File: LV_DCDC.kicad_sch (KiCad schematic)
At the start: 8 parts, among them J1 1017503, J2 1017503

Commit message: made todo, added power
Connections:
- net at R4.2, R5.1, R6.1: no longer C9.1
- net at R6.2: now also C9.1
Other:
- added sheet power (power.kicad_sch)
- sheet CAN ports: added CANH, CANL, RXD, TXD; removed none
- sheet uC ports: added CANRx, CANTx; removed none
- note added: "TODO: BIG DCDC connhector thermistors big decouple V sense and feedback current sense"
- moved on the sheet: C9, R6
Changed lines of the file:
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@@
 	(generator_version "9.0")
 	(paper "A3")
+	(text "TODO:\nBIG DCDC connhector\nthermistors\nbig decouple\nV sense and feedback\ncurrent sense"
+		(exclude_from_sim no)
+		(at 316.738 168.91 0)
+		(effects
+			(font
+				(size 5.08 5.08)
+			)
+		)
+	)
 	(text "BCM4414xG0F4440yzz"
 		(exclude_from_sim no)
@@
 	)
 	(junction
-		(at 295.91 92.71)
-		(diameter 0)
-		(color 0 0 0 0)
-	)
-	(junction
 		(at 240.03 67.31)
 		(diameter 0)
@@
 	)
 	(junction
+		(at 334.01 74.93)
+		(diameter 0)
+		(color 0 0 0 0)
+	)
+	(junction
+		(at 54.61 67.31)
+		(diameter 0)
+		(color 0 0 0 0)
+	)
+	(junction
 		(at 281.94 92.71)
 		(diameter 0)
@@
 	)
 	(junction
-		(at 334.01 74.93)
-		(diameter 0)
-		(color 0 0 0 0)
-	)
-	(junction
-		(at 54.61 67.31)
-		(diameter 0)
-		(color 0 0 0 0)
-	)
-	(junction
 		(at 349.25 67.31)
 		(diameter 0)
@@
 	(wire
 		(pts
+			(xy 281.94 92.71) (xy 293.37 92.71)
+		)
+		(stroke
+			(width 0)
+			(type default)
+		)
+	)
+	(wire
+		(pts
 			(xy 54.61 72.39) (xy 60.96 72.39)
 		)
@@
 	(wire
 		(pts
-			(xy 281.94 96.52) (xy 281.94 92.71)
-		)
-		(stroke
-			(width 0)
-			(type default)
-		)
-	)
-	(wire
-		(pts
-			(xy 295.91 92.71) (xy 295.91 96.52)
-		)
-		(stroke
-			(width 0)
-			(type default)
-		)
-	)
-	(wire
-		(pts
 			(xy 166.37 125.73) (xy 247.65 125.73)
 		)
@@
 	(wire
 		(pts
+			(xy 300.99 92.71) (xy 304.8 92.71)
+		)
+		(stroke
+			(width 0)
+			(type default)
+		)
+	)
+	(wire
+		(pts
 			(xy 43.18 72.39) (xy 54.61 72.39)
 		)
@@
 	(wire
 		(pts
+			(xy 281.94 92.71) (xy 281.94 96.52)
+		)
+		(stroke
+			(width 0)
+			(type default)
+		)
+	)
+	(wire
+		(pts
 			(xy 166.37 67.31) (xy 240.03 67.31)
 		)
@@
 	(wire
 		(pts
-			(xy 295.91 92.71) (xy 303.53 92.71)
+			(xy 360.68 99.06) (xy 368.3 99.06)
 		)
 		(stroke
@@
 	(wire
 		(pts
+			(xy 304.8 92.71) (xy 304.8 96.52)
+		)
+		(stroke
+			(width 0)
+			(type default)
+		)
+	)
+	(wire
+		(pts
 			(xy 29.21 72.39) (xy 43.18 72.39)
 		)
@@
 	(wire
 		(pts
-			(xy 281.94 92.71) (xy 295.91 92.71)
-		)
-		(stroke
-			(width 0)
-			(type default)
-		)
-	)
-	(wire
-		(pts
 			(xy 334.01 64.77) (xy 334.01 67.31)
 		)
@@
 		(pts
 			(xy 344.17 74.93) (xy 349.25 74.93)
+		)
+		(stroke
+			(width 0)
+			(type default)
+		)
+	)
+	(wire
+		(pts
+			(xy 360.68 96.52) (xy 368.3 96.52)
 		)
 		(stroke
@@
 	(symbol
 		(lib_id "Device:C")
-		(at 295.91 100.33 0)
+		(at 304.8 100.33 0)
 		(unit 1)
 		(exclude_from_sim no)
@@
 		(fields_autoplaced yes)
 		(property "Reference" "C9"
-			(at 299.72 99.0599 0)
+			(at 308.61 99.0599 0)
 			(effects
 				(font
@@
 		)
 		(property "Value" "100nF"
-			(at 299.72 101.5999 0)
+			(at 308.61 101.5999 0)
 			(effects
 				(font
@@
 		)
 		(property "Footprint" ""
-			(at 296.8752 104.14 0)
+			(at 305.7652 104.14 0)
 			(effects
 				(font
@@
 		)
 		(property "Datasheet" "~"
-			(at 295.91 100.33 0)
+			(at 304.8 100.33 0)
 			(effects
 				(font
@@
 		)
 		(property "Description" "Unpolarized capacitor"
-			(at 295.91 100.33 0)
+			(at 304.8 100.33 0)
 			(effects
 				(font
@@
 	(symbol
 		(lib_id "power:GND")
-		(at 295.91 104.14 0)
+		(at 304.8 104.14 0)
 		(unit 1)
 		(exclude_from_sim no)
@@
 		(fields_autoplaced yes)
 		(property "Reference" "#PWR026"
-			(at 295.91 110.49 0)
+			(at 304.8 110.49 0)
 			(effects
 				(font
@@
 		)
 		(property "Value" "GND"
-			(at 295.91 109.22 0)
+			(at 304.8 109.22 0)
 			(effects
 				(font
@@
 		)
 		(property "Footprint" ""
-			(at 295.91 104.14 0)
+			(at 304.8 104.14 0)
 			(effects
 				(font
@@
 		)
 		(property "Datasheet" ""
-			(at 295.91 104.14 0)
+			(at 304.8 104.14 0)
 			(effects
 				(font
@@
 		)
 		(property "Description" "Power symbol creates a global label with name \"GND\" , ground"
-			(at 295.91 104.14 0)
+			(at 304.8 104.14 0)
 			(effects
 				(font
@@
 	(symbol
 		(lib_id "Device:R")
-		(at 307.34 92.71 90)
+		(at 297.18 92.71 90)
 		(unit 1)
 		(exclude_from_sim no)
@@
 		(fields_autoplaced yes)
 		(property "Reference" "R6"
-			(at 307.34 86.36 90)
+			(at 297.18 86.36 90)
 			(effects
 				(font
@@
 		)
 		(property "Value" "1k"
-			(at 307.34 88.9 90)
+			(at 297.18 88.9 90)
 			(effects
 				(font
@@
 		)
 		(property "Footprint" ""
-			(at 307.34 94.488 90)
+			(at 297.18 94.488 90)
 			(effects
 				(font
@@
 		)
 		(property "Datasheet" "~"
-			(at 307.34 92.71 0)
+			(at 297.18 92.71 0)
 			(effects
 				(font
@@
 		)
 		(property "Description" "Resistor"
-			(at 307.34 92.71 0)
+			(at 297.18 92.71 0)
 			(effects
 				(font
@@
 	)
 	(sheet
-		(at 337.82 157.48)
-		(size 25.4 16.51)
+		(at 204.47 176.53)
+		(size 13.97 17.78)
 		(exclude_from_sim no)
 		(in_bom yes)
@@
 			(color 0 0 0 0.0000)
 		)
+		(property "Sheetname" "power"
+			(at 204.47 175.8184 0)
+			(effects
+				(font
+					(size 1.27 1.27)
+				)
+				(justify left bottom)
+			)
+		)
+		(property "Sheetfile" "power.kicad_sch"
+			(at 204.47 194.8946 0)
+			(effects
+				(font
+					(size 1.27 1.27)
+				)
+				(justify left top)
+			)
+		)
+		(instances
+			(project "LV_DCDC"
+				(path "/ccad4640-78c7-423b-83df-3ec0b90aa2b3"
+					(page "4")
+				)
+			)
+		)
+	)
+	(sheet
+		(at 368.3 92.71)
+		(size 16.51 10.16)
+		(exclude_from_sim no)
+		(in_bom yes)
+		(on_board yes)
+		(dnp no)
+		(fields_autoplaced yes)
+		(stroke
+			(width 0.1524)
+			(type solid)
+		)
+		(fill
+			(color 0 0 0 0.0000)
+		)
 		(property "Sheetname" "CAN"
-			(at 337.82 156.7684 0)
+			(at 368.3 91.9984 0)
 			(effects
 				(font
@@
 		)
 		(property "Sheetfile" "CAN.kicad_sch"
-			(at 337.82 174.5746 0)
+			(at 368.3 103.4546 0)
 			(effects
 				(font
@@
 				)
 				(justify left top)
+			)
+		)
+		(pin "TXD" input
+			(at 368.3 96.52 180)
+			(effects
+				(font
+					(size 1.27 1.27)
+				)
+				(justify left)
+			)
+		)
+		(pin "CANL" input
+			(at 384.81 99.06 0)
+			(effects
+				(font
+					(size 1.27 1.27)
+				)
+				(justify right)
+			)
+		)
+		(pin "RXD" output
+			(at 368.3 99.06 180)
+			(effects
+				(font
+					(size 1.27 1.27)
+				)
+				(justify left)
+			)
+		)
+		(pin "CANH" input
+			(at 384.81 96.52 0)
+			(effects
+				(font
+					(size 1.27 1.27)
+				)
+				(justify right)
 			)
 		)
@@
 	)
 	(sheet
-		(at 273.05 146.05)
+		(at 337.82 92.71)
 		(size 22.86 20.32)
 		(exclude_from_sim no)
@@
 		)
 		(property "Sheetname" "uC"
-			(at 273.05 145.3384 0)
+			(at 337.82 91.9984 0)
 			(effects
 				(font
@@
 		)
 		(property "Sheetfile" "uC.kicad_sch"
-			(at 273.05 166.9546 0)
+			(at 337.82 113.6146 0)
 			(effects
 				(font
@@
 			)
 		)
+		(pin "CANTx" output
+			(at 360.68 96.52 0)
+			(effects
+				(font
+					(size 1.27 1.27)
+				)
+				(justify right)
+			)
+		)
+		(pin "CANRx" input
+			(at 360.68 99.06 0)
+			(effects
+				(font
+					(size 1.27 1.27)
+				)
+				(justify right)
+			)
+		)

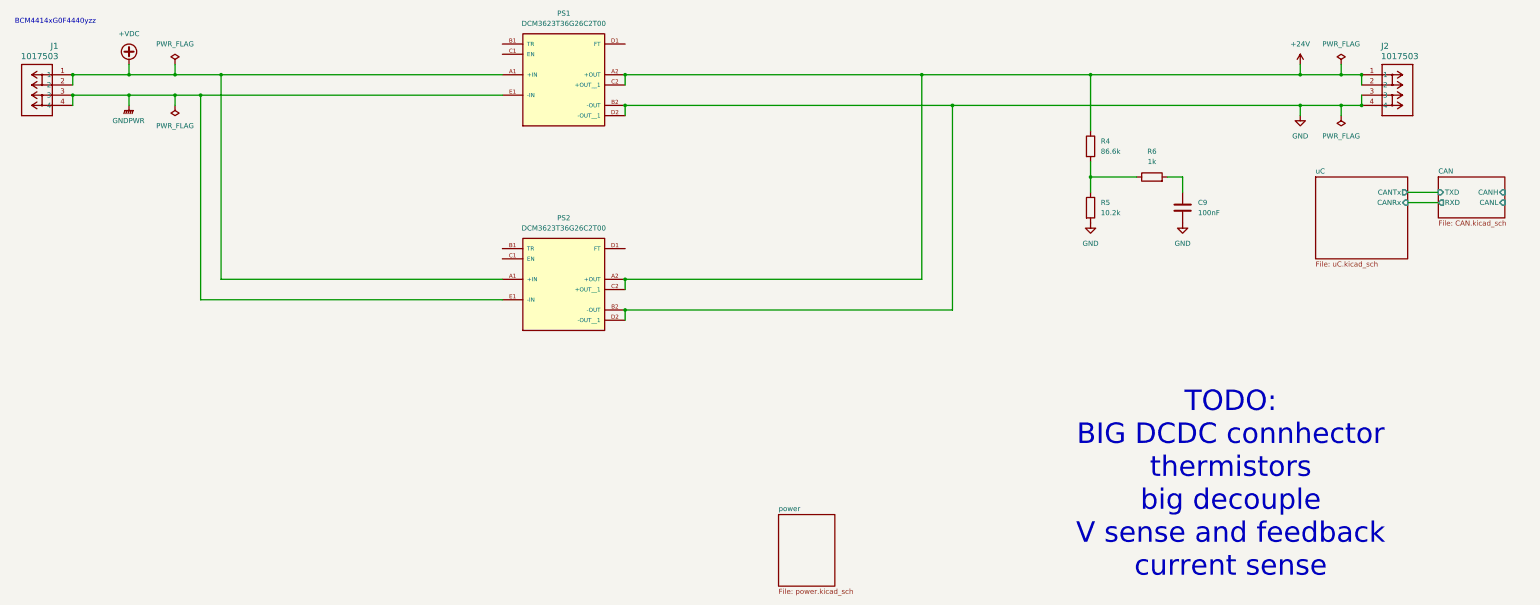
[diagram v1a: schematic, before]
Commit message: fixed bcm connector, added thermistors something else too prolly
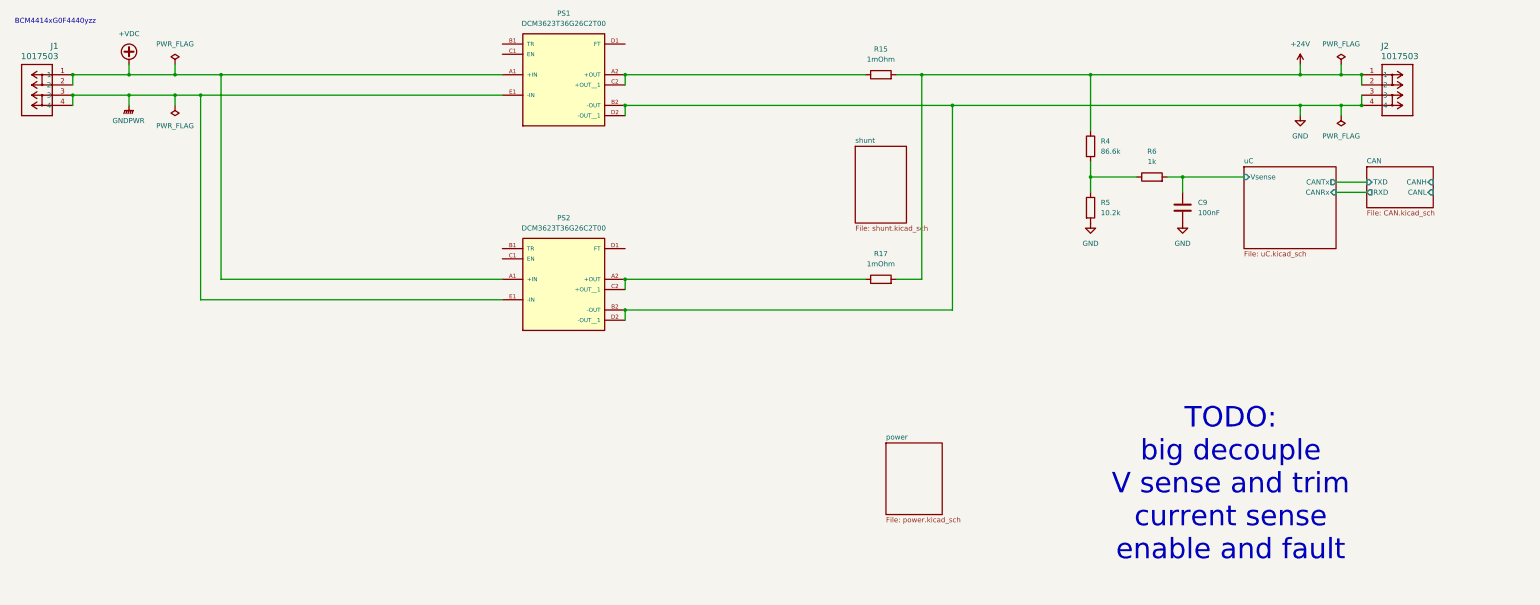
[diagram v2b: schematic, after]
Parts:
- added R15, R17: 1mOhm, symbol Device:R
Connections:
- net +24V: now also R15.2, R17.2; no longer PS1.A2 (+OUT), PS1.C2 (+OUT__1), PS2.A2 (+OUT), PS2.C2 (+OUT__1)
- net uC/Vsense: now reaches C9.1, R6.2
- new net: PS2.A2 (+OUT), PS2.C2 (+OUT__1), R17.1
- new net: PS1.A2 (+OUT), PS1.C2 (+OUT__1), R15.1
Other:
- added sheet shunt (shunt.kicad_sch)
- sheet uC ports: added Vsense; removed none
- note added: "TODO: big decouple V sense and trim current sense enable and fault"
- note removed: "TODO: BIG DCDC connhector thermistors big decouple V sense and feedback current sense"
